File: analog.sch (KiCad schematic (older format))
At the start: 17 parts, among them J10 Conn_01x04_Male, J11 Conn_01x01_Female, J12 Conn_01x01_Female, J13 Conn_01x01_Female, J14 Conn_02x05_Odd_Even, J8 Conn_01x01_Female

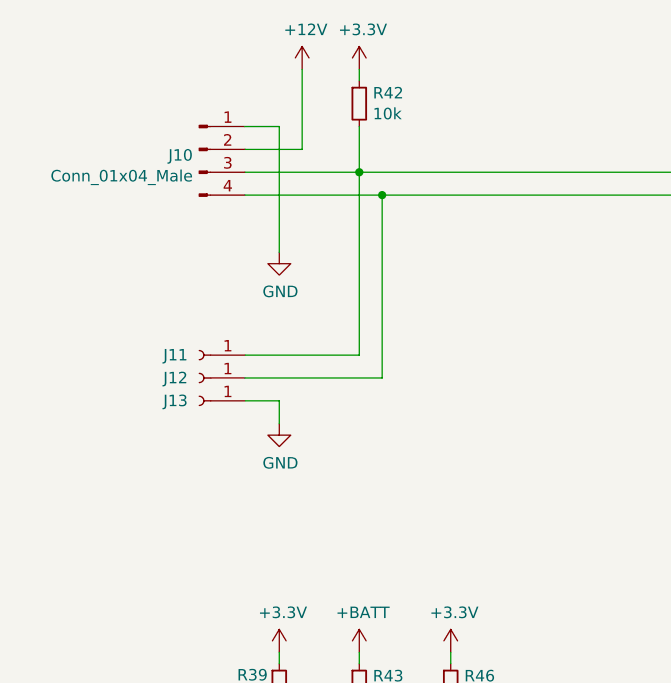
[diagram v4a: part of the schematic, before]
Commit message: LM75 durch TMP411 ersetzt
-Temperatursensor getauscht
-3,3V 2mm Buchse hinzugeügt
-Bohrlöcher wieder eingefügt
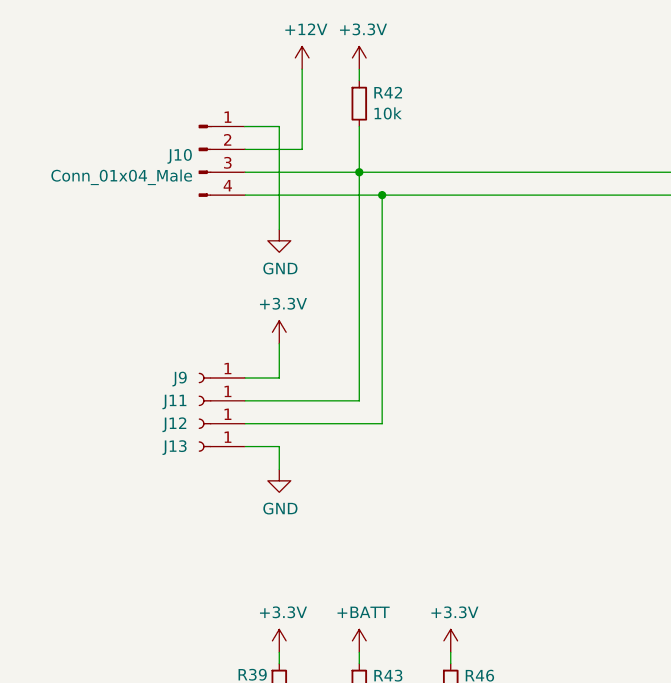
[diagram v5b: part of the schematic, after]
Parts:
- added J9: Conn_01x01_Female, HS-Wismar:2mm_Socket, symbol MCT_Labor_5529-rescue:Conn_01x01_Female-Connector
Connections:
- net +3V3: now also J9.1 (Pin_1)
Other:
- moved on the sheet: J11, J12, J13
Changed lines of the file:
@@
 L MCT_Labor_5529-rescue:GND-power #PWR0192
 U 1 1 5F03480E
-P 2650 2350
-F 0 "#PWR0192" H 2650 2100 50  0001 C CNN
-F 1 "GND" H 2655 2177 50  0000 C CNN
-F 2 "" H 2650 2350 50  0001 C CNN
-F 3 "" H 2650 2350 50  0001 C CNN
-	1    2650 2350
+P 2650 2250
+F 0 "#PWR0192" H 2650 2000 50  0001 C CNN
+F 1 "GND" H 2655 2077 50  0000 C CNN
+F 2 "" H 2650 2250 50  0001 C CNN
+F 3 "" H 2650 2250 50  0001 C CNN
+	1    2650 2250
 	1    0    0    -1
 $EndComp
@@
 Wire Wire Line
 	2500 1800 2650 1800
-Wire Wire Line
-	2650 1800 2650 2350
 $Comp
 L MCT_Labor_5529-rescue:R_Small-Device R42
@@
 $EndComp
 $Comp
-L MCT_Labor_5529-rescue:Conn_01x01_Female-Connector J11
-U 1 1 5F076A07
-P 2300 2800
-F 0 "J11" H 2350 2800 50  0000 L CNN
-F 1 "Conn_01x01_Female" H 2192 2666 50  0001 C CNN
-F 2 "HS-Wismar:2mm_Socket" H 2300 2800 50  0001 C CNN
-F 3 "~" H 2300 2800 50  0001 C CNN
-	1    2300 2800
-	-1   0    0    1
-$EndComp
-$Comp
 L MCT_Labor_5529-rescue:Conn_01x01_Female-Connector J12
 U 1 1 5F077288
-P 2300 2900
-F 0 "J12" H 2350 2900 50  0000 L CNN
-F 1 "Conn_01x01_Female" H 2192 2766 50  0001 C CNN
-F 2 "HS-Wismar:2mm_Socket" H 2300 2900 50  0001 C CNN
-F 3 "~" H 2300 2900 50  0001 C CNN
-	1    2300 2900
+P 2300 3100
+F 0 "J12" H 2350 3100 50  0000 L CNN
+F 1 "Conn_01x01_Female" H 2192 2966 50  0001 C CNN
+F 2 "HS-Wismar:2mm_Socket" H 2300 3100 50  0001 C CNN
+F 3 "~" H 2300 3100 50  0001 C CNN
+	1    2300 3100
 	-1   0    0    1
 $EndComp
@@
 L MCT_Labor_5529-rescue:Conn_01x01_Female-Connector J13
 U 1 1 5F077A2E
-P 2300 3000
-F 0 "J13" H 2350 3000 50  0000 L CNN
-F 1 "Conn_01x01_Female" H 2192 2866 50  0001 C CNN
-F 2 "HS-Wismar:2mm_Socket" H 2300 3000 50  0001 C CNN
-F 3 "~" H 2300 3000 50  0001 C CNN
-	1    2300 3000
+P 2300 3200
+F 0 "J13" H 2350 3200 50  0000 L CNN
+F 1 "Conn_01x01_Female" H 2192 3066 50  0001 C CNN
+F 2 "HS-Wismar:2mm_Socket" H 2300 3200 50  0001 C CNN
+F 3 "~" H 2300 3200 50  0001 C CNN
+	1    2300 3200
 	-1   0    0    1
 $EndComp
 Wire Wire Line
-	2500 2800 3000 2800
-Wire Wire Line
-	3000 2800 3000 2000
-Wire Wire Line
-	2500 2900 3100 2900
-Wire Wire Line
-	3100 2900 3100 2100
+	2500 3000 3000 3000
+Wire Wire Line
+	2500 3100 3100 3100
 Connection ~ 3100 2100
 Wire Wire Line
 	3100 2100 2500 2100
 Wire Wire Line
-	2500 3000 2650 3000
-Wire Wire Line
-	2650 3000 2650 3100
+	2500 3200 2650 3200
+Wire Wire Line
+	2650 3200 2650 3300
 $Comp
 L MCT_Labor_5529-rescue:GND-power #PWR0204
 U 1 1 5F07A1D6
-P 2650 3100
-F 0 "#PWR0204" H 2650 2850 50  0001 C CNN
-F 1 "GND" H 2655 2927 50  0000 C CNN
-F 2 "" H 2650 3100 50  0001 C CNN
-F 3 "" H 2650 3100 50  0001 C CNN
-	1    2650 3100
+P 2650 3300
+F 0 "#PWR0204" H 2650 3050 50  0001 C CNN
+F 1 "GND" H 2655 3127 50  0000 C CNN
+F 2 "" H 2650 3300 50  0001 C CNN
+F 3 "" H 2650 3300 50  0001 C CNN
+	1    2650 3300
 	1    0    0    -1
 $EndComp
@@
 	1    0    0    -1
 $EndComp
+$Comp
+L MCT_Labor_5529-rescue:Conn_01x01_Female-Connector J11
+U 1 1 5F076A07
+P 2300 3000
+F 0 "J11" H 2350 3000 50  0000 L CNN
+F 1 "Conn_01x01_Female" H 2192 2866 50  0001 C CNN
+F 2 "HS-Wismar:2mm_Socket" H 2300 3000 50  0001 C CNN
+F 3 "~" H 2300 3000 50  0001 C CNN
+	1    2300 3000
+	-1   0    0    1
+$EndComp
+$Comp
+L MCT_Labor_5529-rescue:Conn_01x01_Female-Connector J9
+U 1 1 5F2AFB8C
+P 2300 2900
+F 0 "J9" H 2350 2900 50  0000 L CNN
+F 1 "Conn_01x01_Female" H 2192 2766 50  0001 C CNN
+F 2 "HS-Wismar:2mm_Socket" H 2300 2900 50  0001 C CNN
+F 3 "~" H 2300 2900 50  0001 C CNN
+	1    2300 2900
+	-1   0    0    1
+$EndComp
+Wire Wire Line
+	2650 1800 2650 2250
+Wire Wire Line
+	3000 2000 3000 3000
+Wire Wire Line
+	3100 2100 3100 3100
+$Comp
+L power:+3.3V #PWR0101
+U 1 1 5F2B56E3
+P 2650 2750
+F 0 "#PWR0101" H 2650 2600 50  0001 C CNN
+F 1 "+3.3V" H 2665 2923 50  0000 C CNN
+F 2 "" H 2650 2750 50  0001 C CNN
+F 3 "" H 2650 2750 50  0001 C CNN
+	1    2650 2750
+	1    0    0    -1
+$EndComp
+Wire Wire Line
+	2500 2900 2650 2900
+Wire Wire Line
+	2650 2900 2650 2750
 $EndSCHEMATC

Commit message: Aktuell gefertigte Variante
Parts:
- R45: value 2k2 -> 1k
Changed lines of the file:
@@
 P 3000 5850
 F 0 "R45" V 2804 5850 50  0000 C CNN
-F 1 "2k2" V 2895 5850 50  0000 C CNN
+F 1 "1k" V 2895 5850 50  0000 C CNN
 F 2 "Resistor_SMD:R_0603_1608Metric_Pad1.05x0.95mm_HandSolder" H 3000 5850 50  0001 C CNN
 F 3 "~" H 3000 5850 50  0001 C CNN
